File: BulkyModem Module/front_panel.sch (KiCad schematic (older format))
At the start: 37 parts, among them J3 Module_Panel, Q1 2N3904, Q2 2N3904, Q3 2N3904, Q4 2N3904, Q5 2N3904, Q6 2N3904, Q7 2N3904

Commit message: C64 UserPort adapter sketched out (preliminary layout)
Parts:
- added JP7: 232_EN, Connector_PinHeader_2.54mm:PinHeader_1x02_P2.54mm_Vertical, symbol Device:Jumper_NO_Small
- added R21: 10k, resistor:R_Axial_DIN0207_L6.3mm_D2.5mm_P10.16mm_Horizontal, symbol Device:R
- added U2: 74HCT04, Package_DIP:DIP-14_W7.62mm_Socket_LongPads, symbol 74xx:74HCT04
- C10, C11, C7, C8, C9: footprint (none) -> Capacitor_THT:CP_Radial_D5.0mm_P2.00mm
- D2, D8, D9: footprint LED_THT:LED_D5.0mm_Horizontal_O1.27mm_Z3.0mm -> LED_THT:LED_D3.0mm
- D3, D5: footprint (none) -> LED_THT:LED_D3.0mm
- D4: value TX -> RX; footprint (none) -> LED_THT:LED_D3.0mm
- D6: value TX -> CTS; footprint (none) -> LED_THT:LED_D3.0mm
- D7: value TX -> RTS; footprint (none) -> LED_THT:LED_D3.0mm
- J3: footprint (none) -> BulkyModem:Module_Panel
- Q1, Q2, Q3, Q4, Q5, Q6, Q7: footprint Package_TO_SOT_THT:TO-92_Inline -> Package_TO_SOT_THT:TO-92_Inline_Wide
- R1, R10, R11, R12, R13, R14, R2, R3, R5, R6, R7, R8, R9: footprint (none) -> resistor:R_Axial_DIN0207_L6.3mm_D2.5mm_P10.16mm_Horizontal
- R15, R16, R4: footprint Resistor_THT:R_Axial_DIN0207_L6.3mm_D2.5mm_P10.16mm_Horizontal -> resistor:R_Axial_DIN0207_L6.3mm_D2.5mm_P10.16mm_Horizontal
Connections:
- net labels added: LED_C64, LED_CTS, LED_DATA, LED_POW, LED_RS232, LED_RTS, LED_RX, LED_TX
- net labels removed: FP_C64, FP_CTS, FP_DATA, FP_POW, FP_RS232, FP_RTS, FP_RX, FP_TX
- wire segments 115 -> 118
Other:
- note added: "JP7 is intended as a way of enabling\n*one* of the two modes when a front\npanel has not been installed, jumpering\nit will override the switches on the panel."
- moved on the sheet: J3

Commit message: Add DCD
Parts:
- added C16: 22uF, Capacitor_THT:CP_Radial_D5.0mm_P2.00mm, symbol Device:CP_Small
- added D10: DCD, LED_THT:LED_D3.0mm, symbol Device:LED
- added Q8: 2N3904, Package_TO_SOT_THT:TO-92_Inline_Wide, symbol Transistor_BJT:2N3904
- added R24: 10k, resistor:R_Axial_DIN0207_L6.3mm_D2.5mm_P10.16mm_Horizontal, symbol Device:R
- added R25: 470, resistor:R_Axial_DIN0207_L6.3mm_D2.5mm_P10.16mm_Horizontal, symbol Device:R
- D3: value LED -> DATA
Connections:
- net labels added: ESP_DCD, LED_DCD
- wire segments 118 -> 134
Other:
- moved on the sheet: C10, C11, C7, C9, D2, D3, D5, D6, D7, D8, D9, JP7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

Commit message: Initial layout
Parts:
- removed C7: 22uF, Capacitor_THT:CP_Radial_D5.0mm_P2.00mm, symbol Device:CP_Small
- removed Q2, Q3: 2N3904, Package_TO_SOT_THT:TO-92_Inline_Wide, symbol Transistor_BJT:2N3904
- removed R3: 4k7, resistor:R_Axial_DIN0207_L6.3mm_D2.5mm_P10.16mm_Horizontal, symbol Device:R
- removed R5: 10k, resistor:R_Axial_DIN0207_L6.3mm_D2.5mm_P10.16mm_Horizontal, symbol Device:R
- removed R6: 470, resistor:R_Axial_DIN0207_L6.3mm_D2.5mm_P10.16mm_Horizontal, symbol Device:R
- added C20: 22uF, Capacitor_THT:CP_Radial_D5.0mm_P2.00mm, symbol Device:CP_Small
- D3: value DATA -> RI
- R2: value 10k -> 470
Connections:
- net labels added: ESP_RI, LED_RI
- net labels removed: LED_DATA
- wire segments 134 -> 128

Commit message: Tweak schematic in order to fix LEDs and default jumper settings moved to working configuration
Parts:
- removed C10, C11, C16, C20, C8, C9: 22uF, Capacitor_THT:CP_Radial_D5.0mm_P2.00mm, symbol Device:CP_Small
- removed Q1, Q4, Q5, Q6, Q7, Q8: 2N3904, Package_TO_SOT_THT:TO-92_Inline_Wide, symbol Transistor_BJT:2N3904
- removed R1, R11, R13, R24, R7, R9: 10k, resistor:R_Axial_DIN0207_L6.3mm_D2.5mm_P10.16mm_Horizontal, symbol Device:R
- added U5: 74HCT04, Package_DIP:DIP-14_W7.62mm_Socket_LongPads, symbol 74xx:74HCT04
- R10, R12, R14, R2, R25, R8: value 470 -> 1k
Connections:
- wire segments 128 -> 72
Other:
- moved on the sheet: D10, D2, D3, D4, D5, D6, D7, D8, D9, J3, JP7, R10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

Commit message: Layout updated
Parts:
- added D13: STANDBY, LED_THT:LED_D3.0mm, symbol Device:LED
- added R3: 2k2, resistor:R_Axial_DIN0207_L6.3mm_D2.5mm_P10.16mm_Horizontal, symbol Device:R
- JP7: value 232_EN -> 232_SW
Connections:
- net GND: now also R3.1
- net VSB: now reaches J3.17 (VSB)
- net VSB: now also D13.2 (A)
- net LED_STB: now reaches J3.4 (STB)
- net LED_STB: now also D13.1 (K), R3.2
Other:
- moved on the sheet: D2, D8, D9, R15, R16, R4

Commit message: Alternate panel designs
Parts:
- R3, R4: value 2k2 -> 2k2*
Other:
- note added: "* These resistors may have functionally\nbeen replace on the front panel."
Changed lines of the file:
@@
 Comment1 ""
 Comment2 ""
-Comment3 ""
+Comment3 "LED resistor values are suggested safe values, but need to be adjusted for LEDs used."
 Comment4 "Front panel connector as well as circuitry for switches and LEDs."
 $EndDescr
@@
 AR Path="/6390AE73/63B6F359" Ref="R4"  Part="1"
 F 0 "R4" V 2793 3300 50  0000 C CNN
-F 1 "2k2" V 2884 3300 50  0000 C CNN
+F 1 "2k2*" V 2884 3300 50  0000 C CNN
 F 2 "resistor:R_Axial_DIN0207_L6.3mm_D2.5mm_P10.16mm_Horizontal" V 2930 3300 50  0001 C CNN
 F 3 "~" H 3000 3300 50  0001 C CNN
@@
 AR Path="/63D786E4/64BB4F1E" Ref="R?"  Part="1"
 F 0 "R3" V 1868 3300 50  0000 C CNN
-F 1 "2k2" V 1959 3300 50  0000 C CNN
+F 1 "2k2*" V 1959 3300 50  0000 C CNN
 F 2 "resistor:R_Axial_DIN0207_L6.3mm_D2.5mm_P10.16mm_Horizontal" V 2005 3300 50  0001 C CNN
 F 3 "~" H 2075 3300 50  0001 C CNN
@@
 Wire Bus Line
 	6800 1250 6800 2150
+Text Notes 1800 3950 0    50   ~ 0
+* These resistors may have functionally\nbeen replace on the front panel.
 $EndSCHEMATC

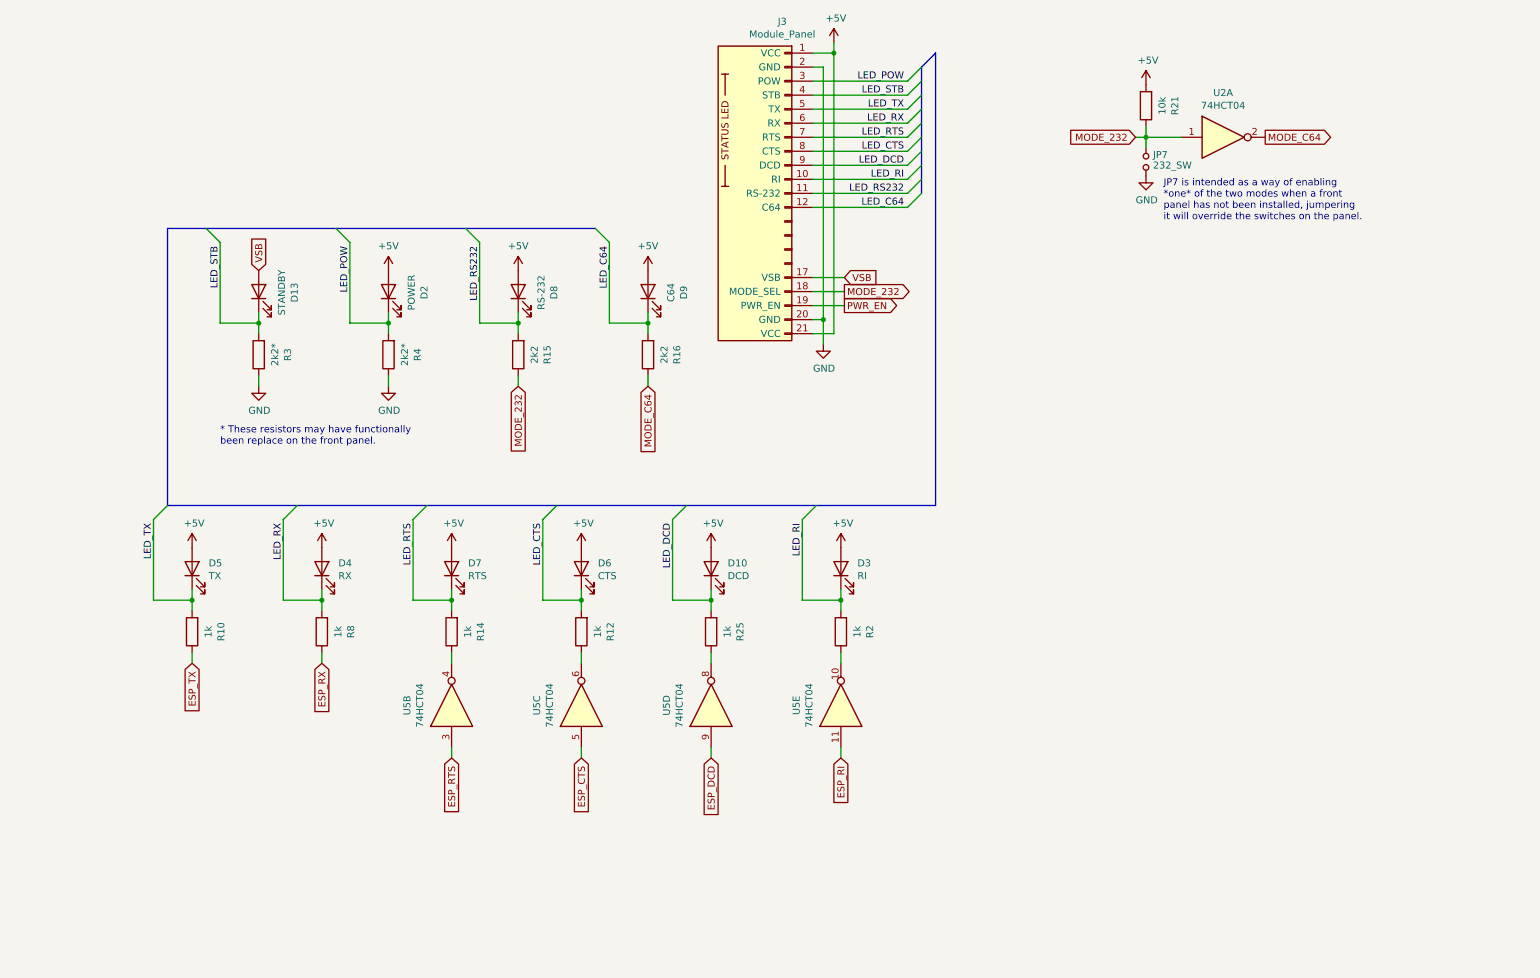
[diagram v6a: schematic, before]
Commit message: Revised version. Mainly buffering signals
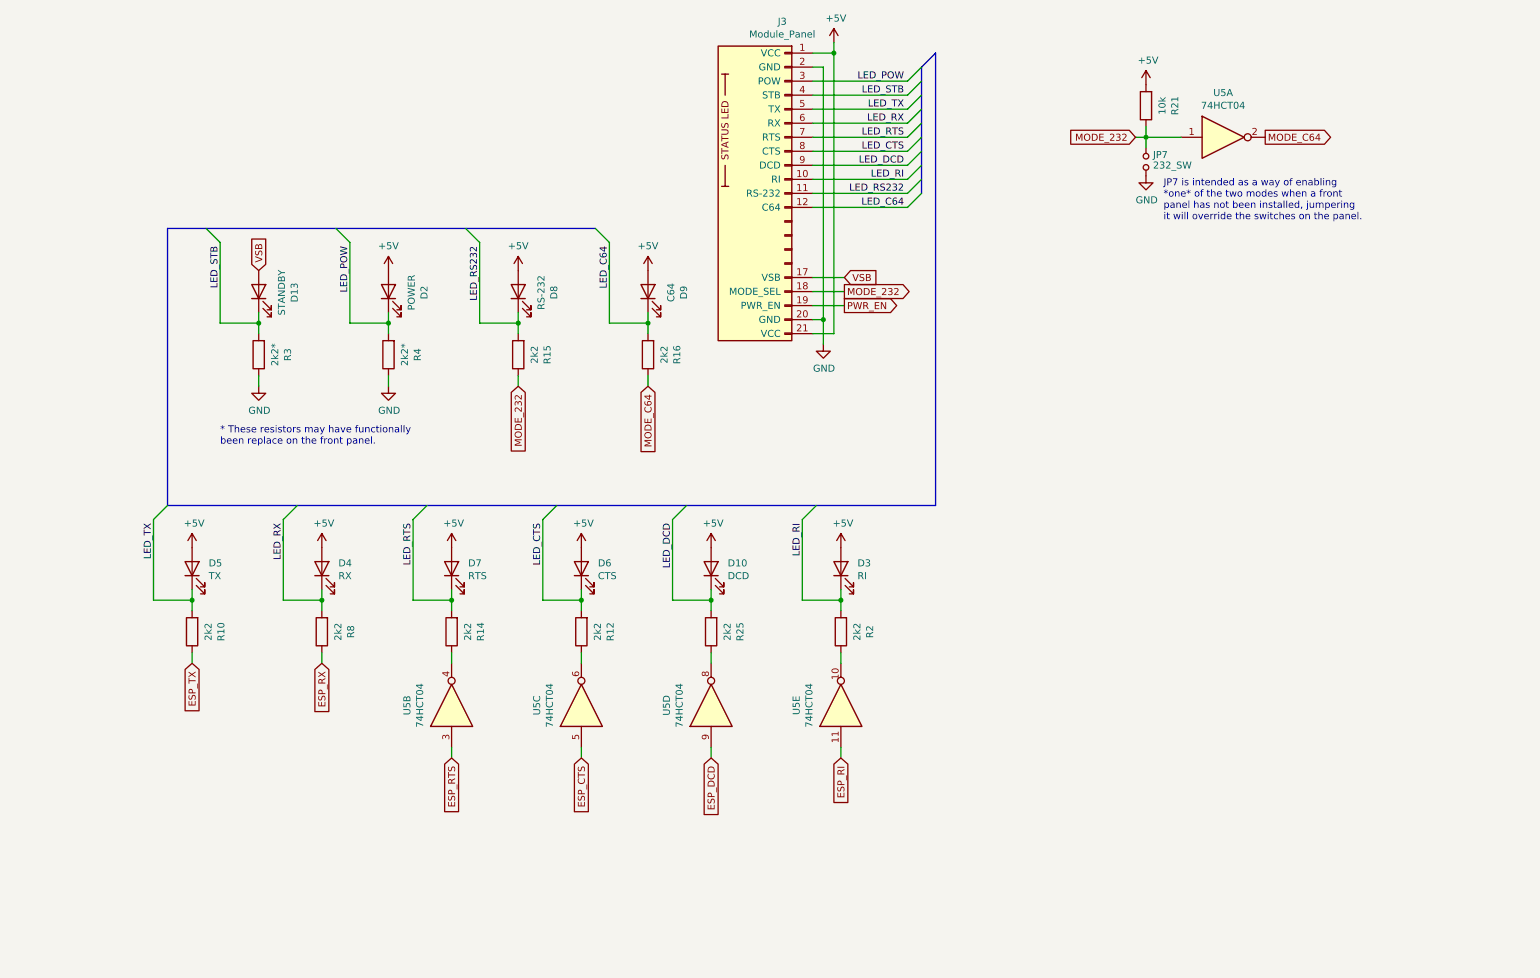
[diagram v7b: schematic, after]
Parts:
- R10, R12, R14, R2, R25, R8: value 1k -> 2k2
- renumbered U2 to U5
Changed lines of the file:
@@
 P 1600 5275
 F 0 "R10" V 1393 5275 50  0000 C CNN
-F 1 "1k" V 1484 5275 50  0000 C CNN
+F 1 "2k2" V 1484 5275 50  0000 C CNN
 F 2 "resistor:R_Axial_DIN0207_L6.3mm_D2.5mm_P10.16mm_Horizontal" V 1530 5275 50  0001 C CNN
 F 3 "~" H 1600 5275 50  0001 C CNN
@@
 P 2525 5275
 F 0 "R8" V 2318 5275 50  0000 C CNN
-F 1 "1k" V 2409 5275 50  0000 C CNN
+F 1 "2k2" V 2409 5275 50  0000 C CNN
 F 2 "resistor:R_Axial_DIN0207_L6.3mm_D2.5mm_P10.16mm_Horizontal" V 2455 5275 50  0001 C CNN
 F 3 "~" H 2525 5275 50  0001 C CNN
@@
 P 4375 5275
 F 0 "R12" V 4168 5275 50  0000 C CNN
-F 1 "1k" V 4259 5275 50  0000 C CNN
+F 1 "2k2" V 4259 5275 50  0000 C CNN
 F 2 "resistor:R_Axial_DIN0207_L6.3mm_D2.5mm_P10.16mm_Horizontal" V 4305 5275 50  0001 C CNN
 F 3 "~" H 4375 5275 50  0001 C CNN
@@
 P 3450 5275
 F 0 "R14" V 3243 5275 50  0000 C CNN
-F 1 "1k" V 3334 5275 50  0000 C CNN
+F 1 "2k2" V 3334 5275 50  0000 C CNN
 F 2 "resistor:R_Axial_DIN0207_L6.3mm_D2.5mm_P10.16mm_Horizontal" V 3380 5275 50  0001 C CNN
 F 3 "~" H 3450 5275 50  0001 C CNN
@@
 P 8950 1750
 AR Path="/62E71FB4" Ref="U?"  Part="1"
-AR Path="/6390AE73/62E71FB4" Ref="U2"  Part="1"
-F 0 "U2" H 8950 2067 50  0000 C CNN
+AR Path="/6390AE73/62E71FB4" Ref="U5"  Part="1"
+F 0 "U5" H 8950 2067 50  0000 C CNN
 F 1 "74HCT04" H 8950 1976 50  0000 C CNN
 F 2 "Package_DIP:DIP-14_W7.62mm_Socket_LongPads" H 8950 1750 50  0001 C CNN
@@
 P 5300 5275
 F 0 "R25" V 5093 5275 50  0000 C CNN
-F 1 "1k" V 5184 5275 50  0000 C CNN
+F 1 "2k2" V 5184 5275 50  0000 C CNN
 F 2 "resistor:R_Axial_DIN0207_L6.3mm_D2.5mm_P10.16mm_Horizontal" V 5230 5275 50  0001 C CNN
 F 3 "~" H 5300 5275 50  0001 C CNN
@@
 P 6225 5275
 F 0 "R2" V 6018 5275 50  0000 C CNN
-F 1 "1k" V 6109 5275 50  0000 C CNN
+F 1 "2k2" V 6109 5275 50  0000 C CNN
 F 2 "resistor:R_Axial_DIN0207_L6.3mm_D2.5mm_P10.16mm_Horizontal" V 6155 5275 50  0001 C CNN
 F 3 "~" H 6225 5275 50  0001 C CNN
@@
 Wire Wire Line
 	6250 2750 6025 2750
+Text Notes 1800 3950 0    50   ~ 0
+* These resistors may have functionally\nbeen replace on the front panel.
 Wire Bus Line
 	1425 2400 4475 2400
@@
 Wire Bus Line
 	6800 1250 6800 2150
-Text Notes 1800 3950 0    50   ~ 0
-* These resistors may have functionally\nbeen replace on the front panel.
 $EndSCHEMATC

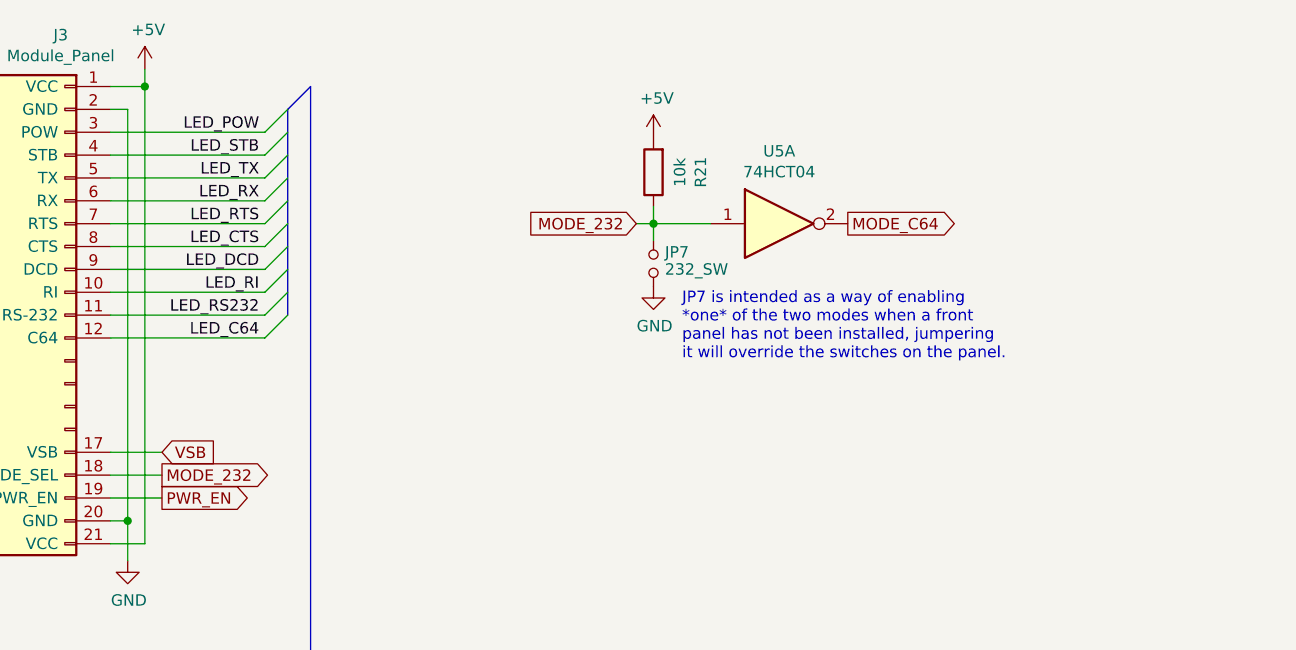
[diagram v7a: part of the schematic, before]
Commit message: Tweaks needed to make revision C actually work.
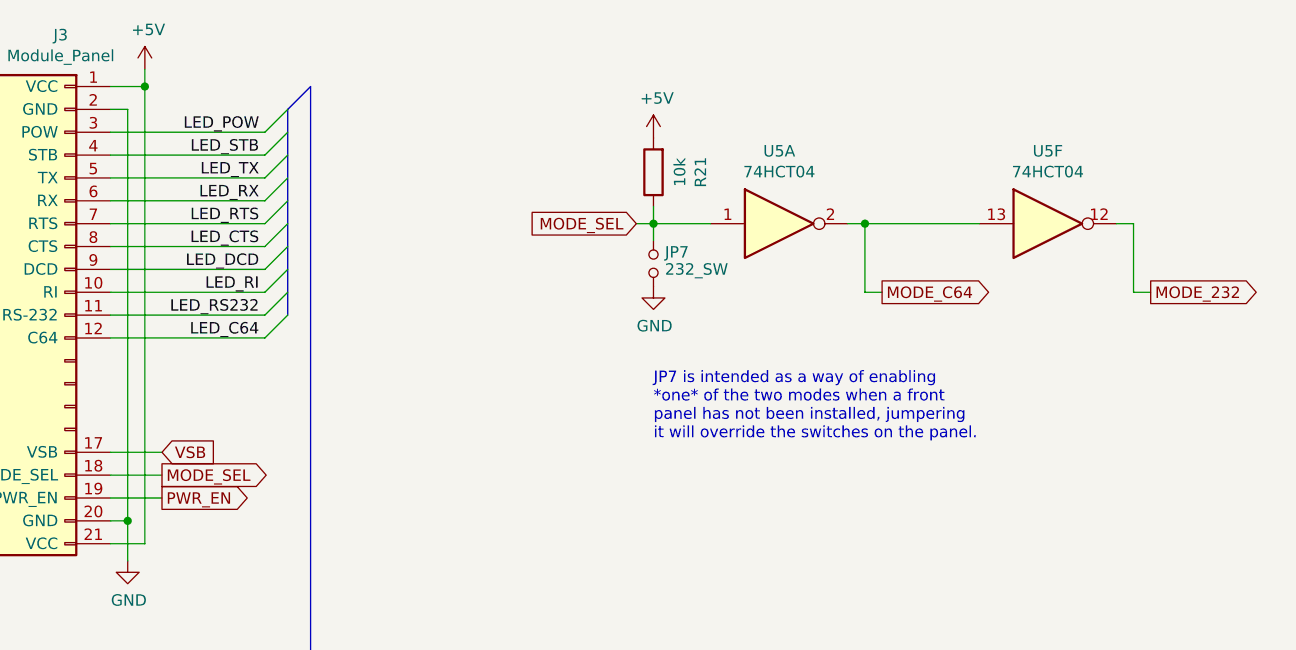
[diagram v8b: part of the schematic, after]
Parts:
- added unit 6 of U5
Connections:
- net MODE_232: now also U5.12; no longer J3.18 (MODE_SEL), JP7.2, R21.1, U5.1
- net MODE_C64: now also U5.13
- new net MODE_SEL: J3.18 (MODE_SEL), JP7.2, R21.1, U5.1
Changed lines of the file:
@@
 Entry Bus Bus
 	6900 1150 6800 1250
-Text GLabel 6250 2850 2    50   Output ~ 0
+Text GLabel 10575 2050 2    50   Output ~ 0
 MODE_232
 Wire Wire Line
@@
 	6250 2850 6025 2850
 Text GLabel 8325 1750 0    50   Input ~ 0
-MODE_232
+MODE_SEL
 $Comp
 L Device:R R21
@@
 Wire Wire Line
 	8400 1825 8400 1750
-Text GLabel 9250 1750 2    50   Output ~ 0
+Text GLabel 9400 2050 2    50   Output ~ 0
 MODE_C64
-Text Notes 8525 2350 0    50   ~ 0
+Text Notes 8400 2700 0    50   ~ 0
 JP7 is intended as a way of enabling\n*one* of the two modes when a front\npanel has not been installed, jumpering\nit will override the switches on the panel.
 Wire Wire Line
@@
 Text Notes 1800 3950 0    50   ~ 0
 * These resistors may have functionally\nbeen replace on the front panel.
+$Comp
+L 74xx:74HCT04 U?
+U 6 1 664EBB40
+P 10125 1750
+AR Path="/664EBB40" Ref="U?"  Part="1"
+AR Path="/6390AE73/664EBB40" Ref="U5"  Part="6"
+AR Path="/63D786E4/664EBB40" Ref="U?"  Part="6"
+F 0 "U5" H 10125 2067 50  0000 C CNN
+F 1 "74HCT04" H 10125 1976 50  0000 C CNN
+F 2 "Package_DIP:DIP-14_W7.62mm_Socket_LongPads" H 10125 1750 50  0001 C CNN
+F 3 "https://assets.nexperia.com/documents/data-sheet/74HC_HCT04.pdf" H 10125 1750 50  0001 C CNN
+	6    10125 1750
+	1    0    0    -1
+$EndComp
+Wire Wire Line
+	9250 1750 9325 1750
+Wire Wire Line
+	9325 1750 9325 2050
+Wire Wire Line
+	9325 2050 9400 2050
+Wire Wire Line
+	10500 1750 10425 1750
+Wire Wire Line
+	9825 1750 9325 1750
+Connection ~ 9325 1750
+Text GLabel 6250 2850 2    50   Output ~ 0
+MODE_SEL
+Wire Wire Line
+	10500 1750 10500 2050
+Wire Wire Line
+	10575 2050 10500 2050
 Wire Bus Line
 	1425 2400 4475 2400
